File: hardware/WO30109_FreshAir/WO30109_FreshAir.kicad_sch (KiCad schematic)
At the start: 76 parts, among them J5 DI 12V/IN1-4/COM/GND, J6 NFC ANT, K1 G5Q-1 DC12, K2 G5Q-1 DC12, K3 G5Q-1 DC12, K4 G5Q-1 DC12, P1 AC IN 230V, P2 PROG, P3 AC OUT, Q1 Si2302CDS, Q2 Si2302CDS, Q3 Si2302CDS, Q4 Si2302CDS, U1 ESP32-C6-WROOM-1-N8, U2 IRM-02-12, U3 SYN480R, U4 AP63203WU-7, U5 TLP290-4, U6 ST25DV04KC-IE6S3, Y1 13.52127MHz 20pF

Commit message: hw(v3.4): F1／P1／P3 改 JLC 代焊；修正端子 CPL 開口方向（J5 原本會朝板內）
使用者 10/07：「要 JLC 那邊都處理完」。
- P1 KEFA KF2EDGR-5.0-2P（C441193）、P3 KF2EDGR-5.08-8P（C441210）：腳距相符；
  規格書建議孔 Ø1.6，封裝與板上孔徑 1.5 → 1.6（焊盤大小不變，市電間距不受影響）
- F1 Littelfuse 37213150411 TR5 T3.15A（C178794）直接焊在 TR5 封裝（腳距 5.08、孔 Ø1.0 符合）；
  不用保險絲座（座子能代焊，但保險絲插進座子要人工）
- make_jlc_files：新增 solve_rotation_by_body()。插拔式端子焊盤一排等距，怎麼轉都對得上，
  依編號求角度會讓開口朝錯邊；改用板上 courtyard 與 JLC 絲印外框比本體方向。
  快取 jlc_footprints.json 多存 JLC 絲印外框（silk）
- 結果：J5 0°→180°（10/5 報價的 CPL 開口朝板內，未下單）、P1 180°、P3 0°（依編號會給 180°）

驗證：ERC 0；DRC 0 錯誤、0 未連線、0 原理圖不一致；test_make_jlc_files 11/11（新增 5 項）；
make_jlc_files --check exit 0；BOM 34 種／68 顆、手焊清單為空；
CPL 與 10/5 版差異只有 J5 角度與新增 F1／P1／P3。

Co-Authored-By: Claude Opus 5.5 (1M context) <noreply@anthropic.com>
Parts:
- F1: value T3.15A 250V -> T3.15A 250V TR5; LCSC (none) -> C178794
- P1: LCSC (none) -> C441193
- P3: LCSC (none) -> C441210

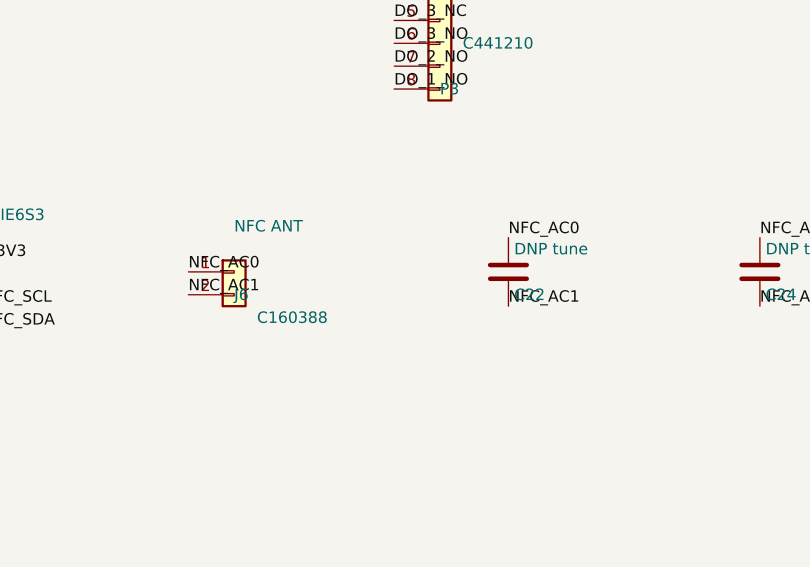
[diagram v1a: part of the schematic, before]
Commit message: hw(v3.4): NFC 天線改插拔（Molex 1462362102＋J6 Micro-Lock Plus 座），C22 上 8.2pF
使用者 10/07：天線「用壓的不要用焊的」、選穩定的。
- 天線 Molex 1462362102：15×25mm、含 ferrite、102mm 雙絞線，線端 505565-0201＋505431-1000（霧錫）；
  DigiKey 庫存 2633、LCSC C3285166（Molex 1462360001-PS／產品頁確認）
- J6：JST SH → Molex 5055680271 直立 SMD（C5350147，鍍錫鉍，和端子同為錫）。新封裝
  WOOW:Molex_MicroLockPlus_505568-0271_1x02_P1.25mm_Vertical（焊盤取自 JLC 封裝）
- C22：La 3.3µH、Ca 4.9pF（PS 表）＋ST25DV 28.5pF → 8.2pF C0G（C1685，諧振約 13.58MHz）；C24 留空微調
- J6 擺放：新座固定腳較寬，原位置固定腳離 P1 市電只有 5.78mm（規則 6.4）且和 J5 courtyard 重疊。
  網格搜尋後改放 (118.5, 112.0) 0°：固定腳 6.63mm；拆掉碰到的 12 段正面走線，
  NFC_AC0／AC1／LED／BOOT 依 DRC 未連線清單用 A* 補線（GND 由鋪銅接通）
- mains_router：沒有網路的銅（MP 固定腳）原本一律當市電（離它 6.5mm），把 J6 自己的訊號腳圍死；
  改交給 is_mains 判斷（繞市電時行為不變，繞低壓時用小間距）
- gen_schematic：C22 有料號時進 BOM
- jlc_footprints.json：C5350147 EasyEDA 抓不下來，焊盤取自同系列 C5356739（其封裝檔名即 5055680271）

驗證：ERC 0；DRC 0 錯誤、0 未連線、0 原理圖不一致（含市電 6.4mm 規則）；
test_make_jlc_files 11/11；make_jlc_files --check exit 0（J6 依 JLC 封裝 180°）；BOM 35 種／69 顆、手焊清單為空。

Co-Authored-By: Claude Opus 5.5 (1M context) <noreply@anthropic.com>
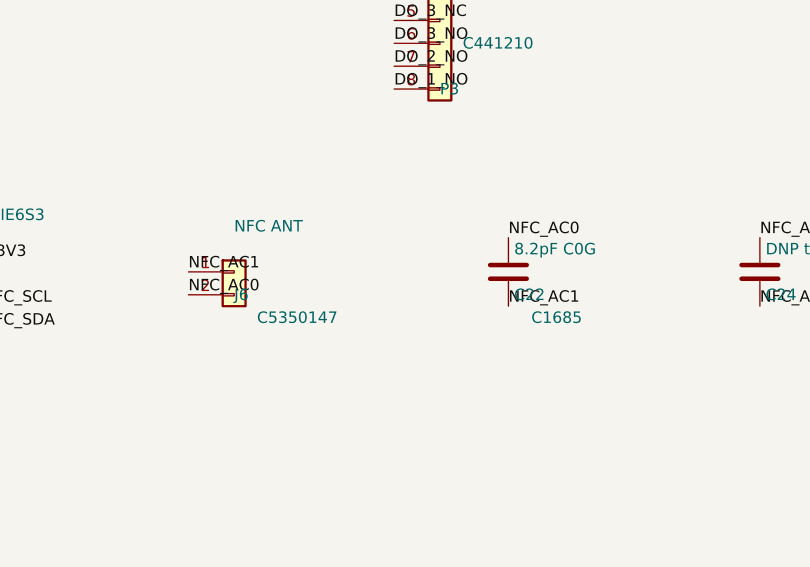
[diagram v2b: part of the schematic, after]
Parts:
- C22: value DNP tune -> 8.2pF C0G; LCSC (none) -> C1685; now in the parts list
- J6: footprint Connector_JST:JST_SH_BM02B-SRSS-TB_1x02-1MP_P1.00mm_Vertical -> WOOW:Molex_MicroLockPlus_505568-0271_1x02_P1.25mm_Vertical; LCSC C160388 -> C5350147
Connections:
- net NFC_AC0: now also J6.2 (Pin_2); no longer J6.1 (Pin_1)
- net NFC_AC1: now also J6.1 (Pin_1); no longer J6.2 (Pin_2)
